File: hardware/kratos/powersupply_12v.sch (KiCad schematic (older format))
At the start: 2 parts, among them U2 MIC29300-12

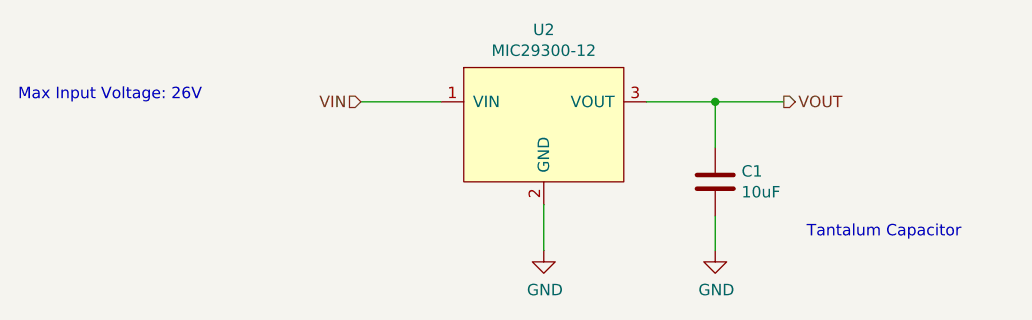
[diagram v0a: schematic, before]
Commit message: Update digikey part numbers in schematics
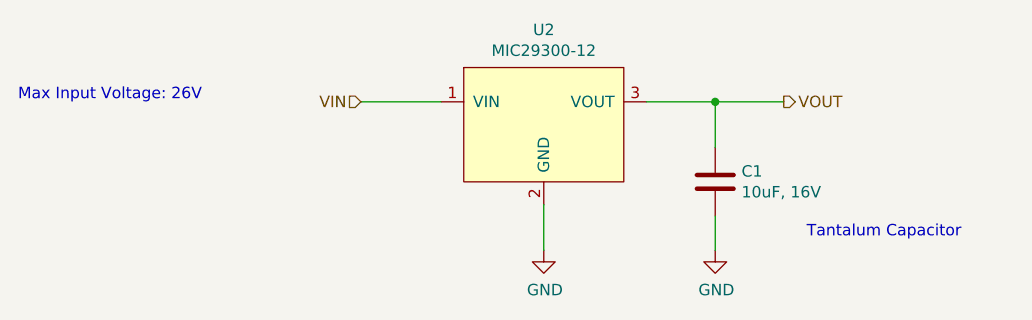
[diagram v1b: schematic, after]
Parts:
- C1: value 10uF -> 10uF, 16V; Digi-Key_PN (none) -> 511-1683-2-ND
- U2: Digi-Key_PN (none) -> 576-2222-ND
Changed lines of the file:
@@
 F 2 "Package_TO_SOT_SMD:TO-263-3_TabPin2" H 5800 2600 50  0001 C CNN
 F 3 "http://ww1.microchip.com/downloads/en/DeviceDoc/MIC2915x-30x-50x-75x-High-Current-Low-Dropout-Regulators-DS20005685B.pdf" H 5750 3450 50  0001 C CNN
+F 4 "576-2222-ND" H 5750 3300 50  0001 C CNN "Digi-Key_PN"
 	1    5750 3300
 	1    0    0    -1
@@
 P 6500 3600
 F 0 "C1" H 6615 3646 50  0000 L CNN
-F 1 "10uF" H 6615 3555 50  0000 L CNN
+F 1 "10uF, 16V" H 6615 3555 50  0000 L CNN
 F 2 "Capacitor_SMD:C_0805_2012Metric" H 6538 3450 50  0001 C CNN
 F 3 "~" H 6500 3600 50  0001 C CNN
+F 4 "511-1683-2-ND" H 6500 3600 50  0001 C CNN "Digi-Key_PN"
 	1    6500 3600
 	1    0    0    -1

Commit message: Update tantalum cap to polarized
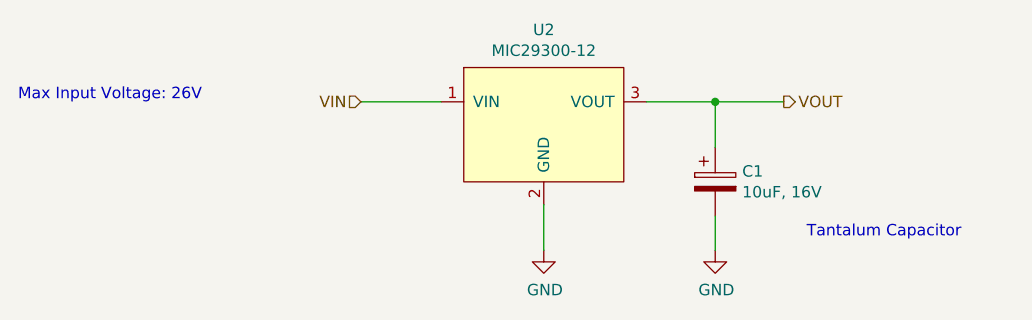
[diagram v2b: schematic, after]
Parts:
- removed C1: 10uF, 16V, Capacitor_SMD:C_0805_2012Metric, symbol Device:C
- added C1: 10uF, 16V, Capacitor_SMD:C_0805_2012Metric, symbol Device:CP
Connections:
- net GND: now also C1.2
- net VOUT: now also C1.1
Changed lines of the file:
@@
 Wire Wire Line
 	4950 3250 5300 3250
-$Comp
-L Device:C C1
-U 1 1 604E58D6
-P 6500 3600
-F 0 "C1" H 6615 3646 50  0000 L CNN
-F 1 "10uF, 16V" H 6615 3555 50  0000 L CNN
-F 2 "Capacitor_SMD:C_0805_2012Metric" H 6538 3450 50  0001 C CNN
-F 3 "~" H 6500 3600 50  0001 C CNN
-F 4 "511-1683-2-ND" H 6500 3600 50  0001 C CNN "Digi-Key_PN"
-	1    6500 3600
-	1    0    0    -1
-$EndComp
 Wire Wire Line
 	6200 3250 6500 3250
@@
 Text Notes 3450 3250 0    50   ~ 0
 Max Input Voltage: 26V
+$Comp
+L Device:CP C1
+U 1 1 6055264E
+P 6500 3600
+F 0 "C1" H 6618 3646 50  0000 L CNN
+F 1 "10uF, 16V" H 6618 3555 50  0000 L CNN
+F 2 "Capacitor_SMD:C_0805_2012Metric" H 6538 3450 50  0001 C CNN
+F 3 "~" H 6500 3600 50  0001 C CNN
+F 4 "511-1683-2-ND" H 6500 3600 50  0001 C CNN "Digi-Key_PN"
+	1    6500 3600
+	1    0    0    -1
+$EndComp
 $EndSCHEMATC
